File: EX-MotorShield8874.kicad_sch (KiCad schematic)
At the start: 74 parts, among them J1 Power, J101 MC 1,5/ 2-G-3,5, J103 MC 1,5/ 2-G-3,5, J105 STEMMA QT, J106 I2C, J107 OLED, J2 Digital/PWM, J3 Analog, J4 Digital/PWM, Q101 AO3400A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

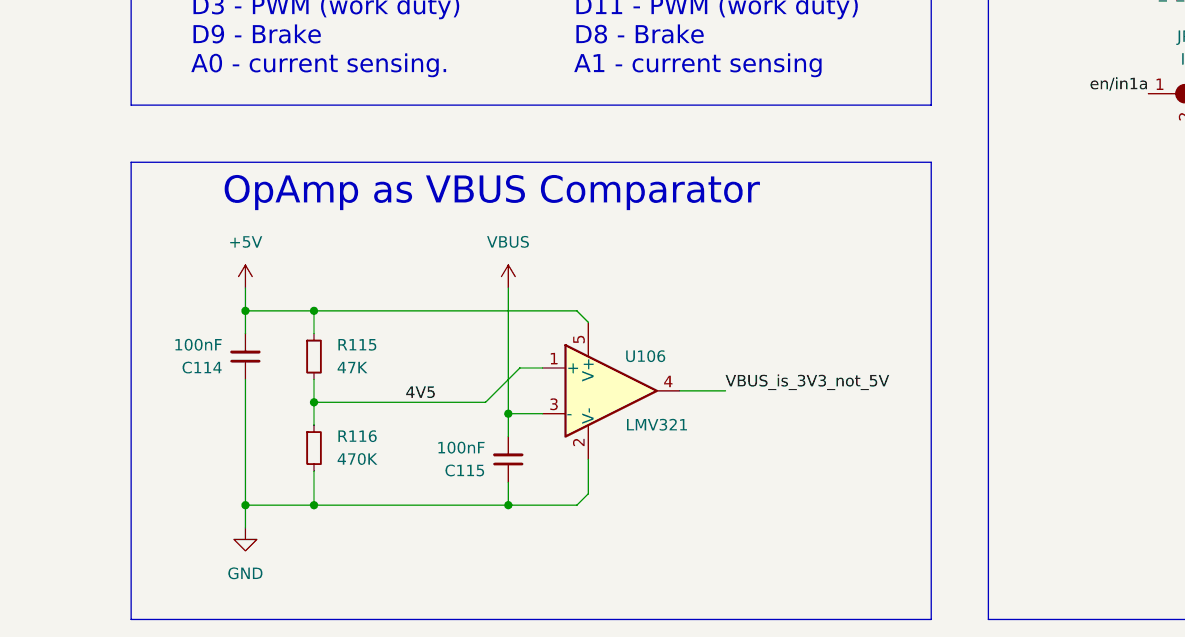
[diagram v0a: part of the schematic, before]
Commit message: Replaced the OpAmp comparitor circuit with a single MOSFET.
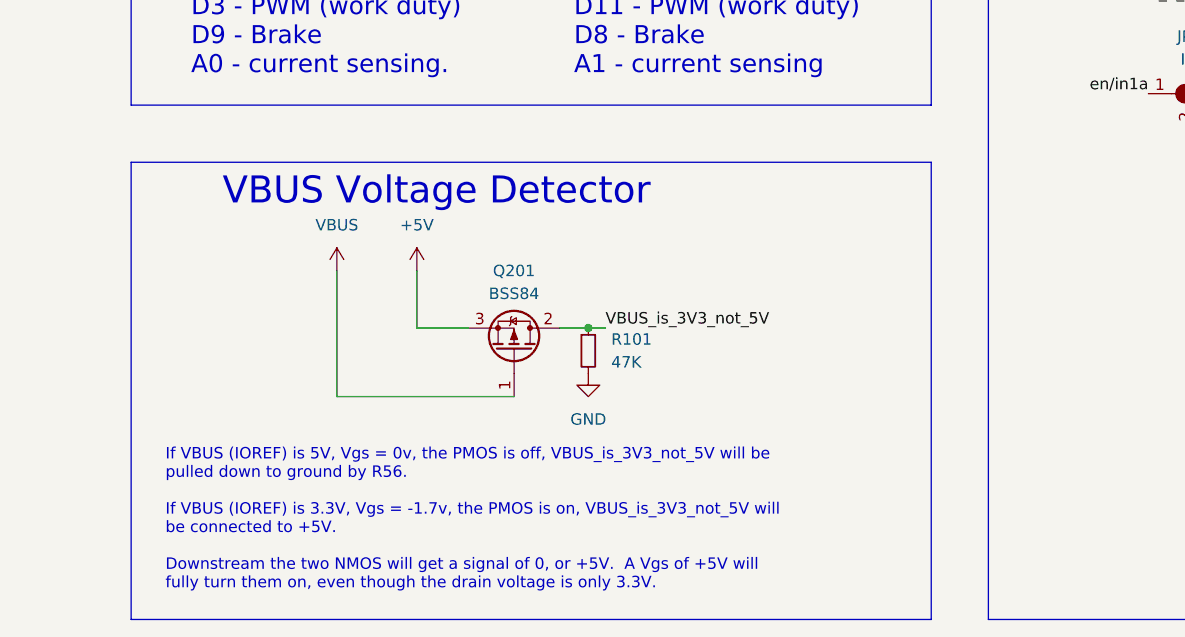
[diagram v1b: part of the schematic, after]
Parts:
- removed C114, C115: 100nF, Capacitor_SMD:C_0402_1005Metric, symbol Device:C_Small
- removed R115: 47K, Resistor_SMD:R_0402_1005Metric, symbol Device:R_Small
- removed R116: 470K, Resistor_SMD:R_0402_1005Metric, symbol Device:R_Small
- removed U106: LMV321, Package_TO_SOT_SMD:SOT-23-5, symbol Amplifier_Operational:LM321
- added Q201: BSS84, Package_TO_SOT_SMD:SOT-23, symbol Transistor_FET:IRF4905
- added R101: 47K, Resistor_SMD:R_0402_1005Metric, symbol Device:R_Small
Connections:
- net +5V: now also Q201.3 (S)
- net GND: now also R101.2
- net VBUS: now also Q201.1 (G)
- net VBUS_is_3V3_not_5V: now also Q201.2 (D), R101.1
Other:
- note added: "If VBUS (IOREF) is 5V, Vgs = 0v, the PMOS is off, VBUS_is_3V3_not_5V will be pulled down to ground by R56. If VBUS (IOREF) is 3.3V, Vgs = -1.7v, the PMOS is on, VBUS_is_3V3_not_5V will be connected to +5V. Downstream the two NMOS will get a signal of 0, or +5V. A Vgs of +5V will fully turn them on, even though the drain voltage is only 3.3V."
- note added: "VBUS Voltage Detector"
- note removed: "OpAmp as VBUS Comparator"
